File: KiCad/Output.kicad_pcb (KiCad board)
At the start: 4 copper layers, 150 x 122 mm, 370 parts, among them J22 EMK_In, J24 Mic_Effekt_In, J25 Mic_Effekt_In, J26 Phono/Line_In, J27 Mic_Effekt_In, J28 Pegel_Out, J29 Pegel_Out, J37 AUX_Send_3, J38 AUX_Send_1, J39 AUX_Send_2, J40 Bass_Out, J41 Kick_Out, J42 Mid_Out, J43 High_Out, J44 Line_Out_L, J45 Line_Out_R, SW10 SW_SPDT, SW11 SW_SPDT, SW12 SW_SPDT, SW3 SW_SPDT, SW4 SW_SPDT, SW5 SW_SPDT, SW6 SW_SPDT, SW7 SW_SPDT, SW8 SW_SPDT, U10 TL074, U11 TL074, U12 TL074, U13 TL074, U14 TL074, U15 TL074, U16 TL074, U17 TL074, U18 TL074, U19 TL074, U20 TL074, U21 TL074, U22 TL074, U8 TL074, U9 TL074

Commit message: PCB Update
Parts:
- moved Z195 5.08 mm to (210.8, 101.6)
- moved Z187 5.08 mm to (210.8, 96.5)
- moved Z203 5.08 mm to (210.8, 99.1)
- moved Z219 3.81 mm to (184.2, 77.5)
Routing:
- net GND_O: track 5.78 -> 295.2 mm, vias 0 -> 100
- net Net-(U20C-+): track 30.7 -> 41.8 mm
- net Net-(U15C--): track 28.3 -> 38.4 mm
- net Net-(U16C--): track 17.1 -> 27.3 mm
- net Net-(U15D--): track 26.4 -> 36.6 mm
- net Net-(U16D--): track 30.0 -> 25.0 mm
- net Net-(R107-Pad1): track 28.2 -> 23.1 mm
- net Net-(Z215-Pad2): track 5.08 -> 7.86 mm
- net Net-(U18D--): track 63.6 -> 65.4 mm
- net Net-(U18C--): track 89.3 -> 91.1 mm
- net Net-(R108-Pad1): track 47.1 -> 48.8 mm
- net Net-(U21C--): track 71.4 -> 70.6 mm
- net Net-(R131-Pad1): track 40.3 -> 39.6 mm, vias 0 -> 1
- net Net-(R62-Pad1): vias 2 -> 3
- added copper zone on B.Cu, net GND_O

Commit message: PCB Update
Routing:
- net Net-(U19C--): track 122.2 -> 113.5 mm
- net Net-(U18C--): track 91.1 -> 84.6 mm
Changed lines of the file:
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@@
 	)
 	(segment
-		(start 183.515 34.925)
-		(end 187.96 39.37)
+		(start 194.945 34.925)
+		(end 199.39 39.37)
 		(width 0.6)
 		(layer "F.Cu")
@@
 	)
 	(segment
-		(start 116.205 34.925)
-		(end 183.515 34.925)
-		(width 0.6)
-		(layer "F.Cu")
-		(net 39)
-	)
-	(segment
-		(start 190.5 60.96)
-		(end 200.66 60.96)
-		(width 0.6)
-		(layer "F.Cu")
-		(net 39)
-	)
-	(segment
-		(start 187.96 39.37)
-		(end 187.96 58.42)
+		(start 199.39 52.07)
+		(end 201.93 54.61)
 		(width 0.6)
 		(layer "F.Cu")
@@
 	)
 	(segment
-		(start 187.96 58.42)
-		(end 190.5 60.96)
+		(start 116.205 34.925)
+		(end 194.945 34.925)
 		(width 0.6)
 		(layer "F.Cu")
@@
 	)
 	(segment
-		(start 203.2 58.42)
-		(end 203.2 57.15)
+		(start 201.93 54.61)
+		(end 203.2 54.61)
 		(width 0.6)
 		(layer "F.Cu")
@@
 	)
 	(segment
-		(start 200.66 60.96)
-		(end 203.2 58.42)
+		(start 199.39 39.37)
+		(end 199.39 52.07)
 		(width 0.6)
 		(layer "F.Cu")
@@
 		(end 165.1 74.93)
 		(width 0.6)
-		(layer "F.Cu")
+		(layer "B.Cu")
 		(net 79)
 	)
@@
 		(end 165.1 74.93)
 		(width 0.6)
-		(layer "F.Cu")
+		(layer "B.Cu")
 		(net 79)
 	)
@@
 	)
 	(segment
-		(start 172.72 151.13)
-		(end 172.72 143.57)
+		(start 182.88 152.4)
+		(end 173.99 152.4)
 		(width 0.6)
 		(layer "F.Cu")
@@
 		(net 87)
 	)
+	(segment
+		(start 172.72 151.13)
+		(end 172.72 143.57)
+		(width 0.6)
+		(layer "F.Cu")
+		(net 87)
+	)
 	(via
-		(at 173.99 152.4)
+		(at 182.88 152.4)
 		(size 0.6)
 		(drill 0.3)
@@
 	)
 	(segment
-		(start 175.47 140.97)
-		(end 172.72 140.97)
-		(width 0.6)
-		(layer "B.Cu")
-		(net 87)
-	)
-	(segment
 		(start 185.09 150.19)
 		(end 185.09 143.51)
@@
 	)
 	(segment
-		(start 173.99 152.4)
-		(end 182.88 152.4)
+		(start 175.47 140.97)
+		(end 172.72 140.97)
 		(width 0.6)
 		(layer "B.Cu")
@@
 		(end 165.1 80.01)
 		(width 0.6)
-		(layer "F.Cu")
+		(layer "B.Cu")
 		(net 103)
 	)
@@
 		(end 165.1 80.01)
 		(width 0.6)
-		(layer "F.Cu")
+		(layer "B.Cu")
 		(net 103)
 	)
@@
 	)
 	(segment
-		(start 159.766 63.246)
-		(end 162.56 66.04)
+		(start 168.91 81.28)
+		(end 170.18 82.55)
 		(width 0.6)
 		(layer "F.Cu")
@@
 	)
 	(segment
-		(start 114.935 62.23)
-		(end 114.935 62.865)
+		(start 117.602 65.532)
+		(end 133.604 65.532)
 		(width 0.6)
 		(layer "F.Cu")
@@
 	)
 	(segment
-		(start 117.094 65.024)
-		(end 134.112 65.024)
-		(width 0.6)
-		(layer "F.Cu")
-		(net 236)
-	)
-	(segment
-		(start 114.935 62.865)
-		(end 117.094 65.024)
-		(width 0.6)
-		(layer "F.Cu")
-		(net 236)
-	)
-	(segment
-		(start 163.83 87.63)
-		(end 171.45 87.63)
+		(start 168.91 66.04)
+		(end 168.91 81.28)
 		(width 0.6)
 		(layer "F.Cu")
@@
 	)
 	(segment
-		(start 135.89 63.246)
-		(end 159.766 63.246)
+		(start 133.604 65.532)
+		(end 135.89 63.246)
 		(width 0.6)
 		(layer "F.Cu")
@@
 	)
 	(segment
-		(start 171.45 87.63)
-		(end 172.72 86.36)
+		(start 114.935 62.865)
+		(end 117.602 65.532)
 		(width 0.6)
 		(layer "F.Cu")
@@
 	)
 	(segment
-		(start 162.56 86.36)
-		(end 163.83 87.63)
+		(start 114.935 62.23)
+		(end 114.935 62.865)
 		(width 0.6)
 		(layer "F.Cu")
@@
 	)
 	(segment
-		(start 134.112 65.024)
-		(end 135.89 63.246)
+		(start 135.89 63.246)
+		(end 166.116 63.246)
 		(width 0.6)
 		(layer "F.Cu")
@@
 	)
 	(segment
-		(start 172.72 86.36)
-		(end 172.72 85.09)
+		(start 170.18 82.55)
+		(end 172.72 82.55)
 		(width 0.6)
 		(layer "F.Cu")
@@
 	)
 	(segment
-		(start 162.56 66.04)
-		(end 162.56 86.36)
+		(start 166.116 63.246)
+		(end 168.91 66.04)
 		(width 0.6)
 		(layer "F.Cu")
@@
 				(xy 140.97 125.73) (xy 140.97 134.62) (xy 140.97 137.16) (xy 147.32 137.16) (xy 147.32 134.62) (xy 143.51 134.62)
 				(xy 143.51 125.73) (xy 173.99 125.73) (xy 173.99 134.62) (xy 172.085 134.62) (xy 172.085 137.16)
-				(xy 177.8 137.16) (xy 177.8 134.62) (xy 177.8 134.62) (xy 177.8 125.73) (xy 205.74 125.73) (xy 205.74 134.62)
-				(xy 201.93 134.62) (xy 201.93 137.16) (xy 208.915 137.16) (xy 209.042 132.08) (xy 212.725 132.08)
-				(xy 212.725 137.16) (xy 210.82 137.16) (xy 210.82 139.7)
+				(xy 177.8 137.16) (xy 177.8 134.62) (xy 177.8 125.73) (xy 205.74 125.73) (xy 205.74 134.62) (xy 201.93 134.62)
+				(xy 201.93 137.16) (xy 208.915 137.16) (xy 209.042 132.08) (xy 212.725 132.08) (xy 212.725 137.16)
+				(xy 210.82 137.16) (xy 210.82 139.7)
 			)
 		)

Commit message: PCB Update
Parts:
- added C119: 10n, Capacitor_SMD:C_1210_3225Metric_Pad1.33x2.70mm_HandSolder, B.Cu at (223.5, 136.5)
- added C120: 100n, Capacitor_SMD:C_0805_2012Metric_Pad1.18x1.45mm_HandSolder, F.Cu at (105.2, 90.4)
- added C121: 100n, Capacitor_SMD:C_0805_2012Metric_Pad1.18x1.45mm_HandSolder, F.Cu at (105.2, 64.5)
- added C122: 100n, Capacitor_SMD:C_0805_2012Metric_Pad1.18x1.45mm_HandSolder, F.Cu at (105.2, 119.6)
- added H10: MountingHole, MountingHole:MountingHole_3.2mm_M3_Pad, F.Cu at (223.5, 40.6)
- added H11: MountingHole, MountingHole:MountingHole_3.2mm_M3_Pad, F.Cu at (88.9, 147.3)
- added H12: MountingHole, MountingHole:MountingHole_3.2mm_M3_Pad, F.Cu at (88.9, 40.6)
- added H9: MountingHole_Pad, MountingHole:MountingHole_3.2mm_M3_Pad, F.Cu at (223.5, 147.3)
- moved R128 2.54 mm to (207.0, 146.1)
- moved C75 2.54 mm to (207.0, 143.5)
- moved R138 2.54 mm to (207.0, 141.0)
- moved Z234 1.27 mm to (168.9, 73.7)
- turned Z242 to 0 degrees
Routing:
- net GND_O: track 295.2 -> 377.5 mm, vias 100 -> 104
- net Net-(U18C--): track 84.6 -> 92.4 mm
- net Net-(U18B-+): track 29.5 -> 21.9 mm
- net Net-(U18A-+): track 29.5 -> 21.9 mm
- net Net-(Z232-Pad2): track 18.6 -> 14.6 mm
- net Net-(U15C-+): track 6.63 -> 8.27 mm
- net Net-(R69-Pad2): track 39.8 -> 38.5 mm
- net Net-(U15B--): track 18.9 -> 17.6 mm
- net Net-(Z234-Pad2): track 16.1 -> 17.3 mm
- net Net-(U18A--): track 5.35 -> 5.88 mm
- added copper zone on In1.Cu, net GND_O
- added copper zone on B.Cu, net Net-(C119-Pad1)

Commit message: PCB Update
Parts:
- removed C120, C121, C122: 100n, Capacitor_SMD:C_0805_2012Metric_Pad1.18x1.45mm_HandSolder
- C119: moved to F.Cu
- moved C119 16.7 mm to (210.8, 147.3), turned to 180 degrees
- moved Z149 5.08 mm to (127.0, 92.7)
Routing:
- net GND_O: track 377.5 -> 327.2 mm, vias 104 -> 105
- net Net-(U19B-+): track 97.3 -> 112.0 mm
- net Net-(U19A-+): track 114.7 -> 127.4 mm
- net Net-(U16C--): track 27.3 -> 38.7 mm
- net Net-(U15D--): track 36.6 -> 48.0 mm
- net Net-(R69-Pad2): track 38.5 -> 47.0 mm
- net Net-(Z143-Pad2): track 5.91 -> 11.0 mm
- net +15V_O: track 79.0 -> 77.0 mm
- net Net-(R62-Pad1): track 50.6 -> 49.9 mm
- net Net-(R61-Pad1): track 5.56 -> 6.09 mm
- net Net-(R63-Pad1): track 57.2 -> 56.7 mm
- net Net-(R131-Pad1): vias 1 -> 0
- added copper zone on F.Cu, net GND_O
- added copper zone on F.Cu, net Net-(C119-Pad1)
- removed copper zone on B.Cu, net Net-(C119-Pad1)

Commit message: PCB Final Update
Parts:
- J22: value EMK_In -> Conn_02x07_Odd_Even; footprint Connector_PinHeader_2.54mm_LongPads:PinHeader_1x05_P2.54mm_Vertical_LongPads -> Connector_PinHeader_2.54mm:PinHeader_2x07_P2.54mm_Vertical
- moved C119 7.96 mm to (217.8, 143.5)
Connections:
- J22 pad 2: +9V_O -> 9V_GND_O
- J22 pad 3: -15V_O -> 9V_GND_O
- J22 pad 4: GND_O -> 9V_GND_O
- J22 pad 5: +15V_O -> +9V_O
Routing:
- net GND_O: track 327.2 -> 394.7 mm, vias 105 -> 103
- net 9V_GND_O: track 0.00 -> 17.3 mm
- net -15V_O: track 82.9 -> 93.0 mm
- net +15V_O: track 77.0 -> 81.5 mm
- net +9V_O: track 0.00 -> 2.54 mm

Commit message: final PCB Update
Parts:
- renumbered C52 to C10, C67 to C104, C79 to C105, C97 to C106, C101 to C107, C105 to C108, C74 to C11, C43 to C12, C62 to C13, C86 to C14, C39 to C15, C49 to C16, C59 to C17, C71 to C18, C83 to C19, C53 to C20, C75 to C21, C42 to C22, C63 to C23, C87 to C24, C38 to C25, C50 to C26, C60 to C27, C72 to C28, C84 to C29, C54 to C30, C76 to C31, C44 to C32, C64 to C34, C88 to C35, C40 to C36, C51 to C38, C61 to C39, C119 to C4, C73 to C40, C85 to C41, C55 to C42, C77 to C43, C45 to C44, C65 to C45, C89 to C46, C41 to C47, C48 to C5, C35 to C50, C37 to C51, C58 to C6, C110 to C66, C68 to C67, C80 to C68, C92 to C69, C70 to C7, C111 to C70, C69 to C71, C81 to C72, C93 to C73, C90 to C74, C94 to C75, C98 to C76, C102 to C77, C106 to C78, C91 to C79, C82 to C8, C95 to C80, C99 to C81, C103 to C82, C107 to C83, C66 to C94, C78 to C95, C100 to C97, C104 to C98, C108 to C99, H12 to H2, H9 to H4, H11 to H5, H10 to H8, J40 to J1, J42 to J10, J43 to J11, J27 to J13, J24 to J15, J38 to J18, J44 to J19, J45 to J21, J25 to J24, J37 to J25, J39 to J26, J28 to J29, J22 to J31, J29 to J32, J26 to J5, J41 to J6, R39 to R1, R117 to R10, R98 to R100, R43 to R107, R57 to R108, R145 to R109, R141 to R11, R33 to R110, R69 to R111, R76 to R112, R44 to R113, R121 to R114, R131 to R115, R79 to R116, R85 to R117, R99 to R118, R51 to R119, R93 to R12, R70 to R120, R100 to R121, R125 to R123, R45 to R124, R58 to R125, R34 to R127, R46 to R128, R77 to R129, R40 to R13, R83 to R130, R123 to R131, R52 to R133, R78 to R136, R124 to R137, R80 to R138, R126 to R139, R49 to R14, R105 to R17, R113 to R18, R127 to R19, R55 to R2, R137 to R20, R146 to R21, R88 to R22, R94 to R23, R41 to R26, R56 to R27, R110 to R28, R134 to R29, R101 to R31, R118 to R34, R142 to R35, R91 to R37, R42 to R38, R50 to R39, R106 to R40, R114 to R41, R128 to R42, R138 to R43, R147 to R44, R87 to R46, R92 to R47, R35 to R48, R53 to R49, R109 to R5, R111 to R50, R135 to R51, R61 to R54, R103 to R55, R36 to R56, R119 to R59, R133 to R6, R143 to R60, R47 to R61, R73 to R63, R95 to R64, R63 to R66, R107 to R68, R115 to R69, R129 to R70, R139 to R71, R148 to R72, R89 to R73, R96 to R74, R37 to R78, R54 to R79, R102 to R8, R112 to R81, R136 to R82, R64 to R83, R104 to R84, R38 to R85, R120 to R86, R144 to R87, R48 to R88, R65 to R89, R74 to R90, R97 to R91, R66 to R92, R108 to R94, R116 to R95, R130 to R96, R140 to R97, R149 to R98, R90 to R99, RV9 to RV1, RV19 to RV10, RV14 to RV12, RV8 to RV14, RV20 to RV15, RV15 to RV16, RV16 to RV19, RV18 to RV2, RV21 to RV20, RV11 to RV21, RV13 to RV3, RV10 to RV5, RV17 to RV6, RV12 to RV7, RV7 to RV8, SW5 to SW1, SW12 to SW10, SW6 to SW3, SW3 to SW4, SW4 to SW5, SW7 to SW6, SW11 to SW7, SW10 to SW9, U8 to U1, U9 to U10, U16 to U12, U18 to U13, U13 to U14, U17 to U16, U10 to U18, U14 to U2, U21 to U20, U22 to U21, U20 to U22, U19 to U3, U12 to U5, U15 to U6, U11 to U7, Z238 to Z1, Z214 to Z101, Z223 to Z102, Z187 to Z103, Z203 to Z104, Z232 to Z105, Z252 to Z106, Z156 to Z107, Z218 to Z108, Z195 to Z110, Z242 to Z111, Z243 to Z114, Z139 to Z115, Z151 to Z116, Z184 to Z117, Z201 to Z118, Z233 to Z119, Z253 to Z120, Z145 to Z121, Z192 to Z122, Z160 to Z123, Z165 to Z124, Z162 to Z125, Z215 to Z126, Z224 to Z127, Z188 to Z128, Z204 to Z129, Z190 to Z13, Z234 to Z130, Z254 to Z131, Z157 to Z132, Z219 to Z133, Z196 to Z138, Z244 to Z139, Z111 to Z141, Z104 to Z147, Z107 to Z148, Z115 to Z149, Z112 to Z153, Z101 to Z159, Z108 to Z160, Z116 to Z161, Z142 to Z162, Z154 to Z163, Z163 to Z164, Z169 to Z165, Z225 to Z166, Z178 to Z167, Z180 to Z168, Z148 to Z169, Z140 to Z17, Z166 to Z170, Z179 to Z171, Z211 to Z172, Z220 to Z173, Z226 to Z174, Z152 to Z18, Z158 to Z182, Z207 to Z183, Z245 to Z184, Z205 to Z185, Z209 to Z186, Z235 to Z187, Z255 to Z188, Z143 to Z195, Z155 to Z196, Z246 to Z197, Z149 to Z198, Z236 to Z199, Z146 to Z20, Z256 to Z200, Z109 to Z205, Z176 to Z208, Z208 to Z209, Z102 to Z214, Z105 to Z215, Z113 to Z216, Z119 to Z217, Z121 to Z218, Z175 to Z219, Z177 to Z220, Z206 to Z221, Z210 to Z222, Z117 to Z223, Z257 to Z231, Z118 to Z233, Z258 to Z234, Z259 to Z235, Z120 to Z236, Z212 to Z24, Z221 to Z25, Z185 to Z28, Z198 to Z29, Z182 to Z3, Z227 to Z30, Z247 to Z31, Z216 to Z34, Z193 to Z36, Z237 to Z37, Z110 to Z39, Z199 to Z4, Z103 to Z43, Z106 to Z44, Z114 to Z45, Z239 to Z46, Z181 to Z47, Z197 to Z48, Z229 to Z52, Z249 to Z53, Z189 to Z56, Z141 to Z60, Z153 to Z61, Z147 to Z64, Z213 to Z65, Z222 to Z66, Z186 to Z68, Z202 to Z69, Z228 to Z7, Z230 to Z70, Z250 to Z71, Z217 to Z74, Z194 to Z77, Z240 to Z78, Z248 to Z8, Z241 to Z81, Z138 to Z82, Z150 to Z83, Z183 to Z84, Z200 to Z85, Z231 to Z88, Z251 to Z89, Z144 to Z90, Z191 to Z91, Z159 to Z92, Z164 to Z93, Z161 to Z96
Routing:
- net GND_O: track 394.7 -> 327.2 mm
- net -15V_O: track 93.0 -> 41.6 mm
- net +15V_O: track 81.5 -> 41.6 mm
- net Net-(U6C--): track 38.4 -> 51.1 mm
- net Net-(U16B--): track 22.0 -> 34.5 mm
- net 9V_GND_O: track 17.3 -> 10.2 mm
- net Net-(R31-Pad2): track 13.8 -> 9.52 mm
- net Net-(R84-Pad2): track 13.9 -> 9.59 mm
- net Net-(R8-Pad2): track 15.2 -> 11.4 mm
- net Net-(R55-Pad2): track 14.3 -> 10.5 mm

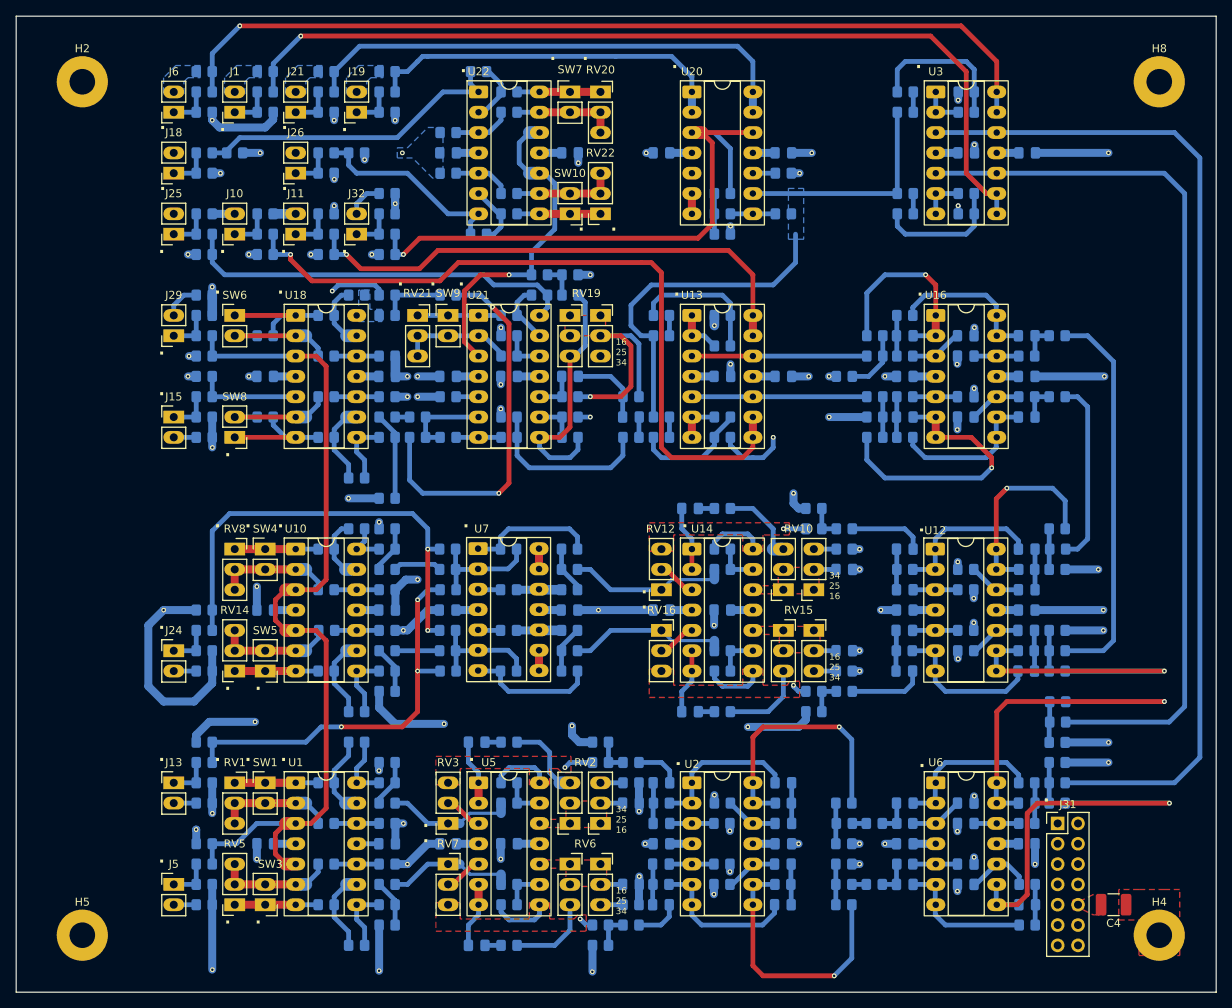
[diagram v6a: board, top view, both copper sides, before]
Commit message: Output phasen korrektur durch invertierender verstärker
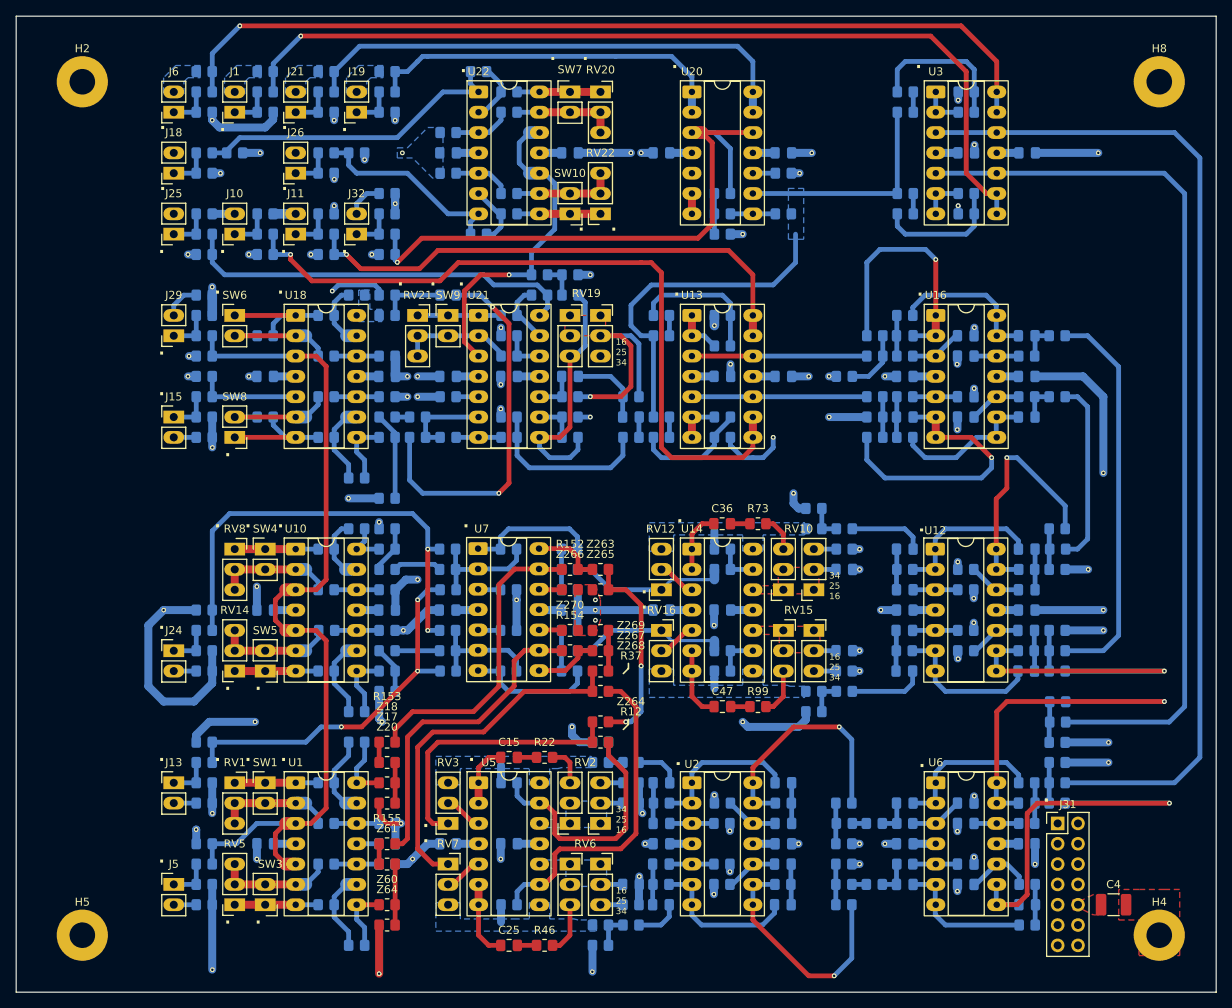
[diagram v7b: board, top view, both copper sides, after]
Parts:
- added R152: 10k, Resistor_SMD:R_0805_2012Metric_Pad1.20x1.40mm_HandSolder, F.Cu at (149.9, 101.6)
- added R153: 10k, Resistor_SMD:R_0805_2012Metric_Pad1.20x1.40mm_HandSolder, F.Cu at (127.0, 123.2)
- added R154: 10k, Resistor_SMD:R_0805_2012Metric_Pad1.20x1.40mm_HandSolder, F.Cu at (149.9, 111.8)
- added R155: 10k, Resistor_SMD:R_0805_2012Metric_Pad1.20x1.40mm_HandSolder, F.Cu at (127.0, 135.9)
- added Z263: ~, Resistor_SMD:R_0805_2012Metric_Pad1.20x1.40mm_HandSolder, F.Cu at (153.7, 101.6)
- added Z264: ~, Resistor_SMD:R_0805_2012Metric_Pad1.20x1.40mm_HandSolder, F.Cu at (153.7, 120.7)
- added Z265: ~, Resistor_SMD:R_0805_2012Metric_Pad1.20x1.40mm_HandSolder, F.Cu at (153.7, 104.1)
- added Z266: ~, Resistor_SMD:R_0805_2012Metric_Pad1.20x1.40mm_HandSolder, F.Cu at (149.9, 104.1)
- added Z267: ~, Resistor_SMD:R_0805_2012Metric_Pad1.20x1.40mm_HandSolder, F.Cu at (153.7, 111.8)
- added Z268: ~, Resistor_SMD:R_0805_2012Metric_Pad1.20x1.40mm_HandSolder, F.Cu at (153.7, 114.3)
- added Z269: ~, Resistor_SMD:R_0805_2012Metric_Pad1.20x1.40mm_HandSolder, F.Cu at (153.7, 109.2)
- added Z270: ~, Resistor_SMD:R_0805_2012Metric_Pad1.20x1.40mm_HandSolder, F.Cu at (149.9, 109.2)
- C15, C25, C36, C47, R12, R22, R37, R46, R73, R99, Z17, Z18, Z20, Z60, Z61, Z64: moved to F.Cu
- moved R37 26.7 mm to (153.7, 116.8)
- moved R12 13.7 mm to (153.7, 123.2)
- moved Z18 5.08 mm to (127.0, 125.7), turned to 180 degrees
- moved Z20 5.08 mm to (127.0, 130.8)
- moved R22 4.84 mm to (146.7, 125.1)
- moved R73 4.84 mm to (173.4, 95.9)
- moved R99 4.49 mm to (173.4, 118.7)
- moved C15 4.47 mm to (142.2, 125.1)
- moved R46 4.44 mm to (146.7, 148.6)
- moved C36 4.44 mm to (168.9, 95.9)
- moved C47 4.09 mm to (168.9, 118.7)
- moved C25 4.04 mm to (142.2, 148.6)
- moved Z61 2.54 mm to (127.0, 138.4), turned to 180 degrees
- turned Z125 to 0 degrees
- turned Z96 to 0 degrees
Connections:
- U7 pad 10: GND_O -> Net-(U7C-+)
- U7 pad 12: GND_O -> Net-(U7D-+)
- U7 pad 14: Net-(U7D--) -> Net-(R152-Pad2)
- U7 pad 8: Net-(U7C--) -> Net-(R154-Pad2)
- Z18 pad 2: Net-(R12-Pad1) -> Net-(R153-Pad1)
- Z61 pad 2: Net-(R37-Pad1) -> Net-(R155-Pad1)
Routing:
- net Net-(U7C--): track 2.54 -> 40.2 mm
- net Net-(U5C--): track 5.35 -> 41.1 mm
- net Net-(U7D--): track 2.54 -> 38.2 mm
- net Net-(R37-Pad1): track 16.1 -> 44.6 mm
- net Net-(U5D--): track 5.35 -> 31.2 mm
- net Net-(Z263-Pad2): track 0.00 -> 25.4 mm, vias 0 -> 2
- net Net-(R12-Pad1): track 16.1 -> 34.7 mm
- net GND_O: track 327.2 -> 343.6 mm, vias 103 -> 105
- net Net-(R8-Pad2): track 11.4 -> 2.18 mm, vias 1 -> 0
- net Net-(R152-Pad2): track 0.00 -> 8.74 mm
- net Net-(R154-Pad2): track 0.00 -> 8.24 mm
- net Net-(R55-Pad2): track 10.5 -> 2.27 mm, vias 1 -> 0
- net Net-(R84-Pad2): track 9.59 -> 2.17 mm, vias 1 -> 0
- net Net-(R31-Pad2): track 9.52 -> 2.18 mm, vias 1 -> 0
- net Net-(U16A--): track 24.6 -> 31.3 mm
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- added copper zone on B.Cu, net Net-(R31-Pad2)
- added copper zone on B.Cu, net Net-(R55-Pad2)
- added copper zone on B.Cu, net Net-(R8-Pad2)
- added copper zone on B.Cu, net Net-(R84-Pad2)
- added copper zone on B.Cu, net Net-(U5C-+)
- added copper zone on B.Cu, net Net-(U5D-+)
- removed copper zone on F.Cu, net Net-(R31-Pad2)
- removed copper zone on F.Cu, net Net-(R55-Pad2)
- removed copper zone on F.Cu, net Net-(R8-Pad2)
- removed copper zone on F.Cu, net Net-(R84-Pad2)
- removed copper zone on F.Cu, net Net-(U5C-+)
- removed copper zone on F.Cu, net Net-(U5D-+)

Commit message: Output Stage in phase gebracht
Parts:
- added R156: 10k, Resistor_SMD:R_0805_2012Metric_Pad1.20x1.40mm_HandSolder, B.Cu at (161.3, 54.6)
- added R157: 10k, Resistor_SMD:R_0805_2012Metric_Pad1.20x1.40mm_HandSolder, B.Cu at (168.9, 54.6)
- added Z271: ~, Resistor_SMD:R_0805_2012Metric_Pad1.20x1.40mm_HandSolder, B.Cu at (161.3, 52.1)
- added Z272: ~, Resistor_SMD:R_0805_2012Metric_Pad1.20x1.40mm_HandSolder, B.Cu at (161.3, 41.9)
- added Z273: ~, Resistor_SMD:R_0805_2012Metric_Pad1.20x1.40mm_HandSolder, B.Cu at (161.3, 47.0)
- added Z274: ~, Resistor_SMD:R_0805_2012Metric_Pad1.20x1.40mm_HandSolder, B.Cu at (161.3, 44.5)
- moved R125 3.81 mm to (119.4, 90.2)
- moved R49 3.81 mm to (119.4, 96.5)
- moved Z166 2.54 mm to (168.9, 59.7)
- moved Z173 2.54 mm to (168.9, 62.2)
- moved Z174 2.54 mm to (168.9, 57.1)
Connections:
- U20 pad 5: GND_O -> Net-(U20B-+)
- U20 pad 7: Net-(U20B--) -> Net-(R156-Pad2)
- Z174 pad 2: Net-(U20A-+) -> Net-(R157-Pad1)
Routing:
- net Net-(R156-Pad2): track 0.00 -> 22.3 mm
- net Net-(U20A-+): track 77.1 -> 68.6 mm
- net Net-(Z272-Pad2): track 0.00 -> 5.91 mm
- net Net-(U20B--): track 2.54 -> 5.62 mm
- net Net-(U20B-+): track 0.00 -> 2.81 mm
- net Net-(R157-Pad1): track 0.00 -> 2.54 mm
- net Net-(R125-Pad1): track 8.30 -> 9.96 mm
- net Net-(R49-Pad2): track 5.76 -> 7.42 mm
- net GND_O: track 343.6 -> 342.3 mm, vias 105 -> 106
- net Net-(R109-Pad1): track 5.62 -> 6.67 mm
